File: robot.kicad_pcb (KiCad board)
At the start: 2 copper layers, 21.3 x 25.4 mm, 8 parts, among them IC1 A3901SEJTR-T, J1 MOT1_OUTPUT, J2 MOT2_OUTPUT, J3 CONN_BAT, U1 MOUDLE-SEEEDUINO-XIAO-ESP32C3

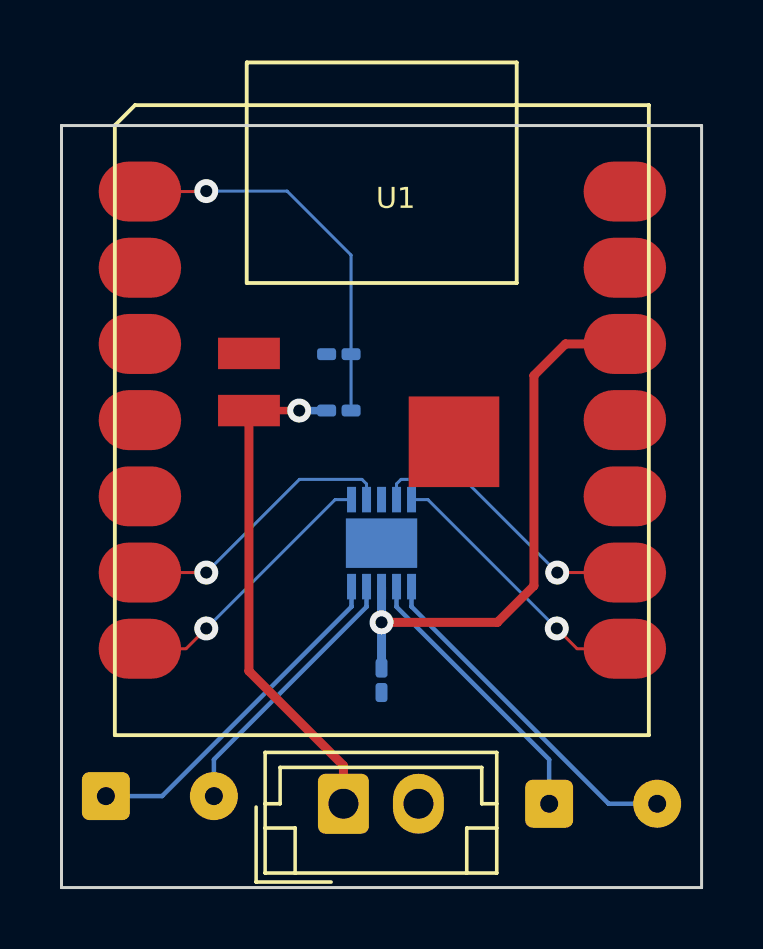
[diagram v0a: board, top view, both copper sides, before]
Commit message: add power switch and battery voltage divider
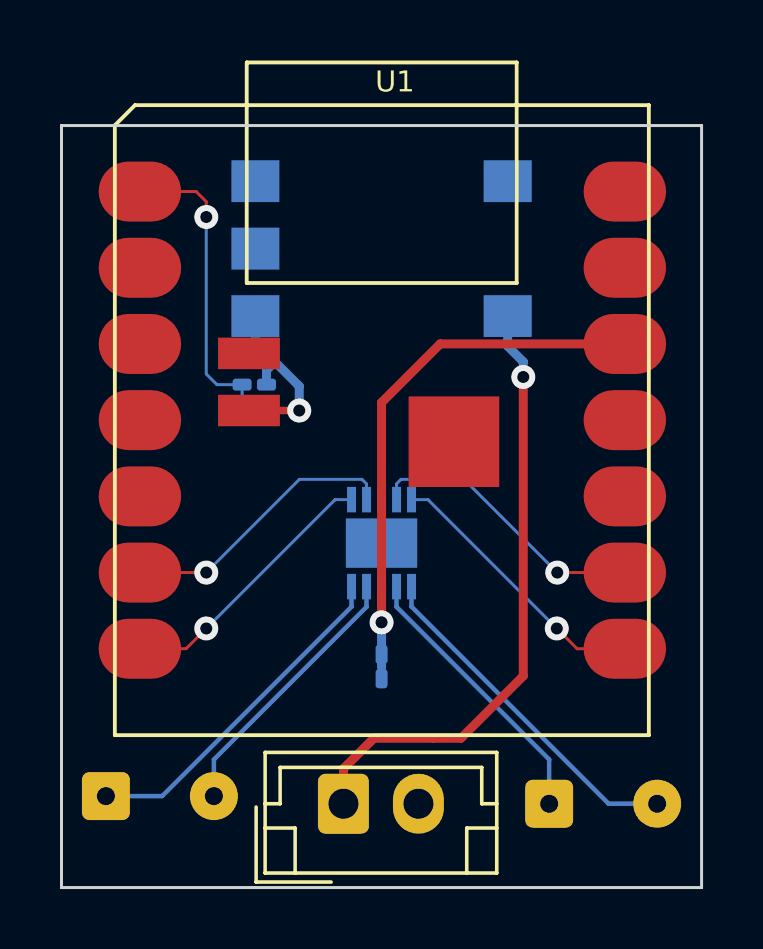
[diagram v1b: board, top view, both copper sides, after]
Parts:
- added S1: FSM1LP, FSM1LP:FSM1LP, B.Cu at (430.5, 72.7)
- moved R2 3.48 mm to (426.3, 78.2), turned to 0 degrees
- moved R1 2.95 mm to (426.3, 77.2), turned to 180 degrees
- moved C1 0.46 mm to (430.5, 86.6)
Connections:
- R1 pad 1: +BATT -> VCC
- U1 pad 16: +BATT -> VCC
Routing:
- net VCC: track 0.00 -> 6.31 mm, vias 0 -> 1
- net +BATT: track 17.0 -> 20.7 mm
- net Net-(U1-PA02_A0_D0): track 13.2 -> 10.4 mm

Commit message: 6-switch dipswitch for misc. configuration
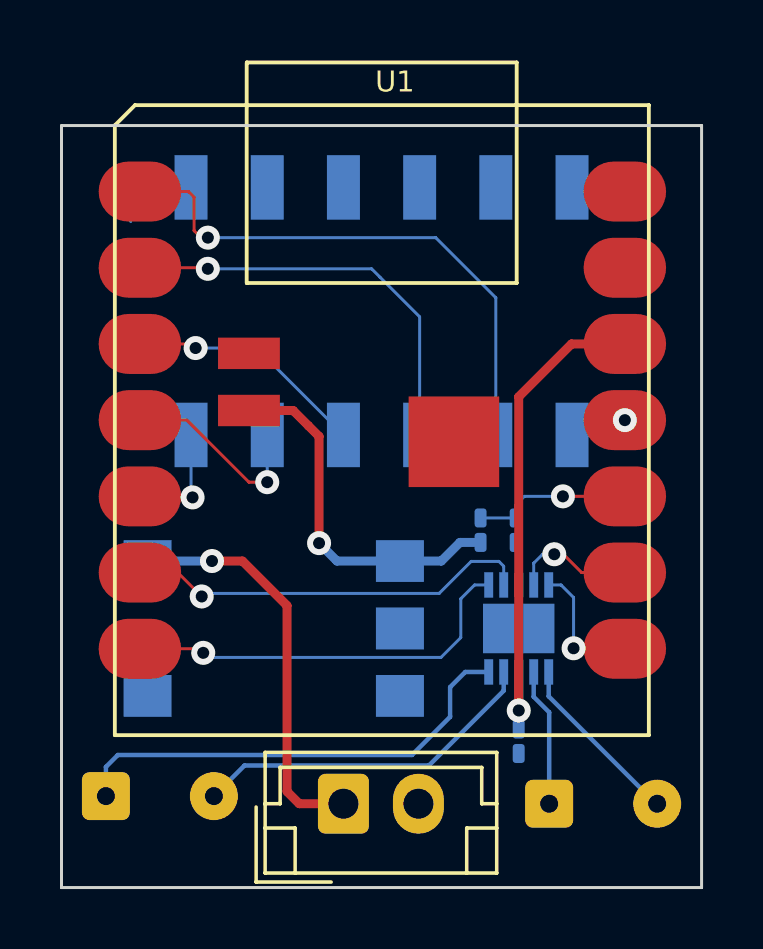
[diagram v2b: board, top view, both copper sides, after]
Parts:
- added S3: A6SN-6101, A6SN-6101:A6SN6101, B.Cu at (430.5, 74.8)
- IC1: footprint KiCad:SON50P300X300X75-11N-D -> A3901SEJTR-T:SON50P300X300X75-11N-D
- moved S1 13.2 mm to (426.9, 85.3), turned to 0 degrees
- moved R2 9.52 mm to (435.0, 82.1), turned to -90 degrees
- moved R1 8.97 mm to (433.8, 82.1), turned to 90 degrees
- moved IC1 5.38 mm to (435.1, 85.3)
- moved C1 5.21 mm to (435.1, 89.1)
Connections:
- R1 pad 2: Net-(U1-PA02_A0_D0) -> /BATT_MEAS
- R2 pad 1: Net-(U1-PA02_A0_D0) -> /BATT_MEAS
- U1 pad 1: Net-(U1-PA02_A0_D0) -> /BTN_2
- U1 pad 10: unconnected-(U1-PA5_A9_D9_MISO-Pad10) -> /BATT_MEAS
- U1 pad 11: unconnected-(U1-PA6_A10_D10_MOSI-Pad11) -> /BTN_1
- U1 pad 2: unconnected-(U1-PA4_A1_D1-Pad2) -> /BTN_3
- U1 pad 3: unconnected-(U1-PA10_A2_D2-Pad3) -> /BTN_4
- U1 pad 4: unconnected-(U1-PA11_A3_D3-Pad4) -> /BTN_5
- U1 pad 5: unconnected-(U1-PA8_A4_D4_SDA-Pad5) -> /BTN_6
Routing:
- net /BTN_2: track 0.00 -> 18.9 mm, vias 0 -> 1
- net /BTN_3: track 0.00 -> 13.9 mm, vias 0 -> 1
- net Net-(U1-PA02_A0_D0): track 10.4 -> 0.00 mm, vias 1 -> 0
- net /BTN_4: track 0.00 -> 8.04 mm, vias 0 -> 1
- net +BATT: track 20.7 -> 13.5 mm
- net /BTN_5: track 0.00 -> 6.68 mm, vias 0 -> 1
- net VCC: track 6.31 -> 12.1 mm
- net /MOT2_OUT2: track 11.6 -> 5.91 mm
- net /BATT_MEAS: track 0.00 -> 5.36 mm, vias 0 -> 1
- net /MOT2_IN1: track 9.48 -> 4.14 mm
- net /MOT2_IN2: track 9.17 -> 4.41 mm
- net /MOT2_OUT1: track 9.34 -> 4.62 mm
- net /MOT1_IN1: track 9.11 -> 13.5 mm
- net /MOT1_IN2: track 9.43 -> 13.6 mm
- net /MOT1_OUT1: track 11.5 -> 15.6 mm
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
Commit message: 4-switch dipswitch, LEDs, reorder
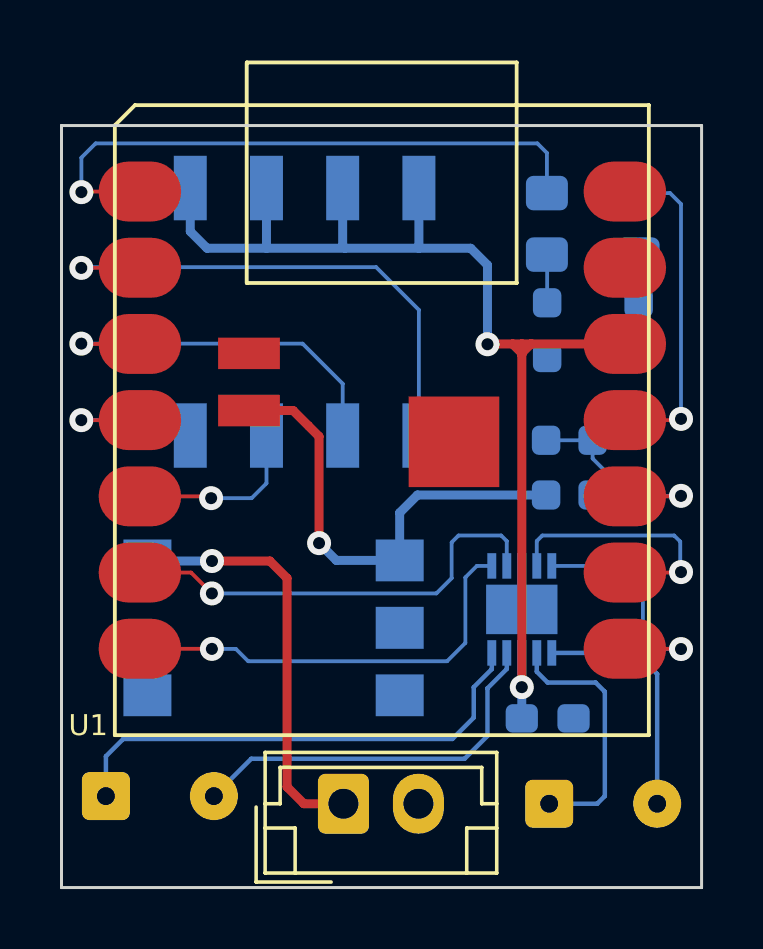
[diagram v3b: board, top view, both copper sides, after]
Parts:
- removed S3: A6SN-6101, A6SN-6101:A6SN6101
- added D1: LED, LED_SMD:LED_0805_2012Metric_Pad1.15x1.40mm_HandSolder, B.Cu at (436.0, 71.9)
- added D2: LED, LED_SMD:LED_0805_2012Metric_Pad1.15x1.40mm_HandSolder, B.Cu at (439.1, 71.9)
- added R3: R, Resistor_SMD:R_0603_1608Metric_Pad0.98x0.95mm_HandSolder, B.Cu at (436.1, 75.4)
- added R4: R, Resistor_SMD:R_0603_1608Metric_Pad0.98x0.95mm_HandSolder, B.Cu at (439.1, 75.4)
- added S2: A6SN-4101, A6SN-4101:A6SN4101, B.Cu at (428.0, 74.8)
- C1: footprint Capacitor_SMD:C_0201_0603Metric_Pad0.64x0.40mm_HandSolder -> Capacitor_SMD:C_0603_1608Metric_Pad1.08x0.95mm_HandSolder
- IC1: footprint A3901SEJTR-T:SON50P300X300X75-11N-D -> KiCad:SON50P300X300X75-11N-D
- R1: footprint Capacitor_SMD:C_0201_0603Metric_Pad0.64x0.40mm_HandSolder -> Resistor_SMD:R_0603_1608Metric_Pad0.98x0.95mm_HandSolder
- R2: footprint Resistor_SMD:R_0201_0603Metric_Pad0.64x0.40mm_HandSolder -> Resistor_SMD:R_0603_1608Metric_Pad0.98x0.95mm_HandSolder
- moved R2 3.31 mm to (437.6, 80.0)
- moved R1 3.02 mm to (436.0, 80.0)
- moved C1 1.23 mm to (436.1, 88.3), turned to 0 degrees
- moved IC1 0.64 mm to (435.2, 84.7)
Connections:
- U1 pad 1: /BTN_2 -> /LED_R
- U1 pad 11: /BTN_1 -> /LED_L
- U1 pad 2: /BTN_3 -> /BTN_1
- U1 pad 3: /BTN_4 -> /BTN_2
- U1 pad 4: /BTN_5 -> /BTN_4
- U1 pad 5: /BTN_6 -> /BTN_3
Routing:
- net +3.3V: track 16.6 -> 39.7 mm, vias 1 -> 2
- net /LED_R: track 0.00 -> 20.6 mm, vias 0 -> 1
- net /BTN_1: track 1.96 -> 17.9 mm
- net /LED_L: track 0.00 -> 10.7 mm, vias 0 -> 1
- net /BTN_3: track 13.9 -> 6.04 mm
- net /BTN_5: track 6.68 -> 0.00 mm, vias 1 -> 0
- net /BTN_2: track 18.9 -> 12.9 mm
- net /MOT2_IN1: track 4.14 -> 8.64 mm
- net /MOT2_IN2: track 4.41 -> 8.43 mm
- net /MOT2_OUT1: track 4.62 -> 8.61 mm
- net /BTN_6: track 3.87 -> 0.00 mm, vias 1 -> 0
- net VCC: track 12.1 -> 15.9 mm
- net Net-(D2-K): track 0.00 -> 3.48 mm
- net /BTN_4: track 8.04 -> 5.74 mm
- net /MOT2_OUT2: track 5.91 -> 8.13 mm
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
